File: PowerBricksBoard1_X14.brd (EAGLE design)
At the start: 76.2 x 50.8 mm, 16 parts

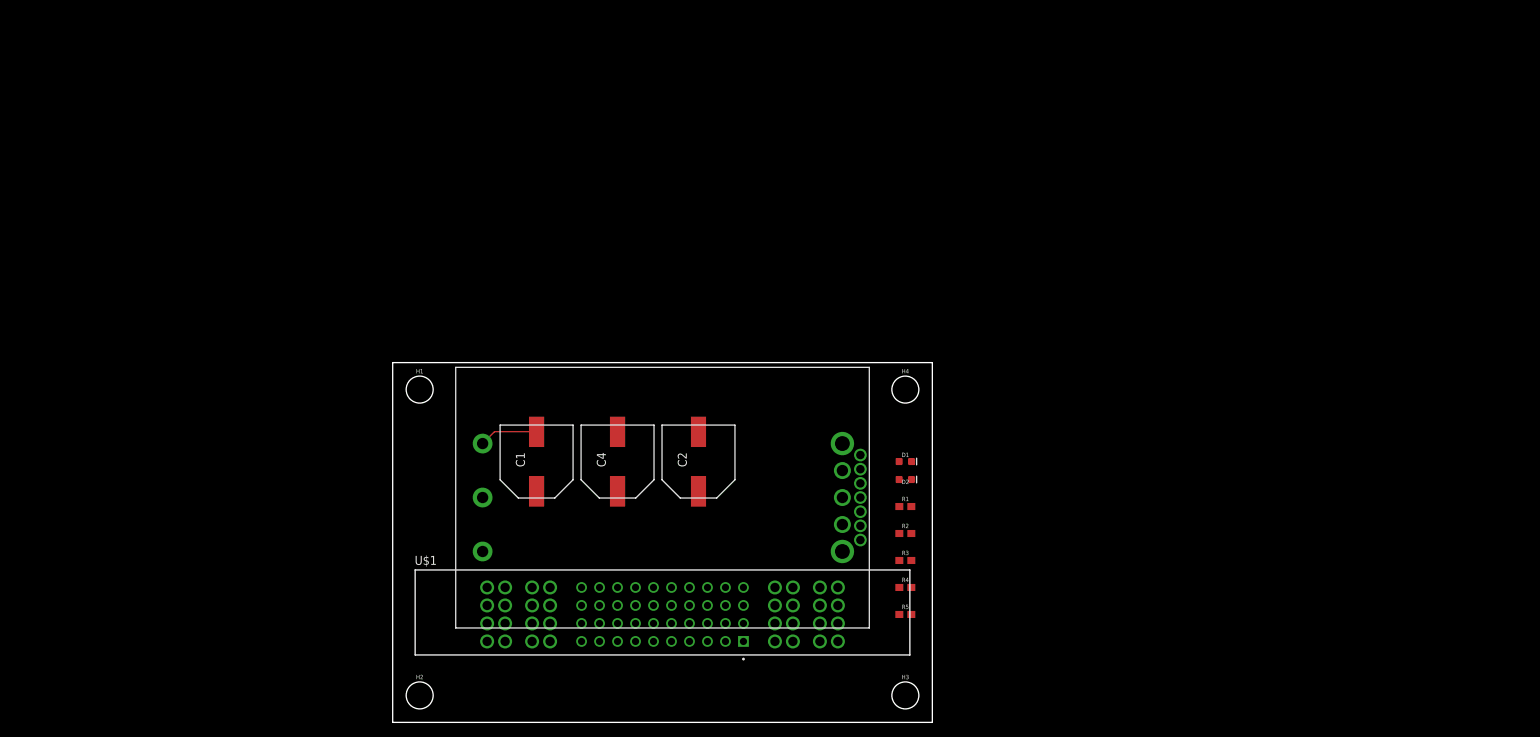
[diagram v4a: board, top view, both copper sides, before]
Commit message: I deleted the old board and made a new one with the connector type.
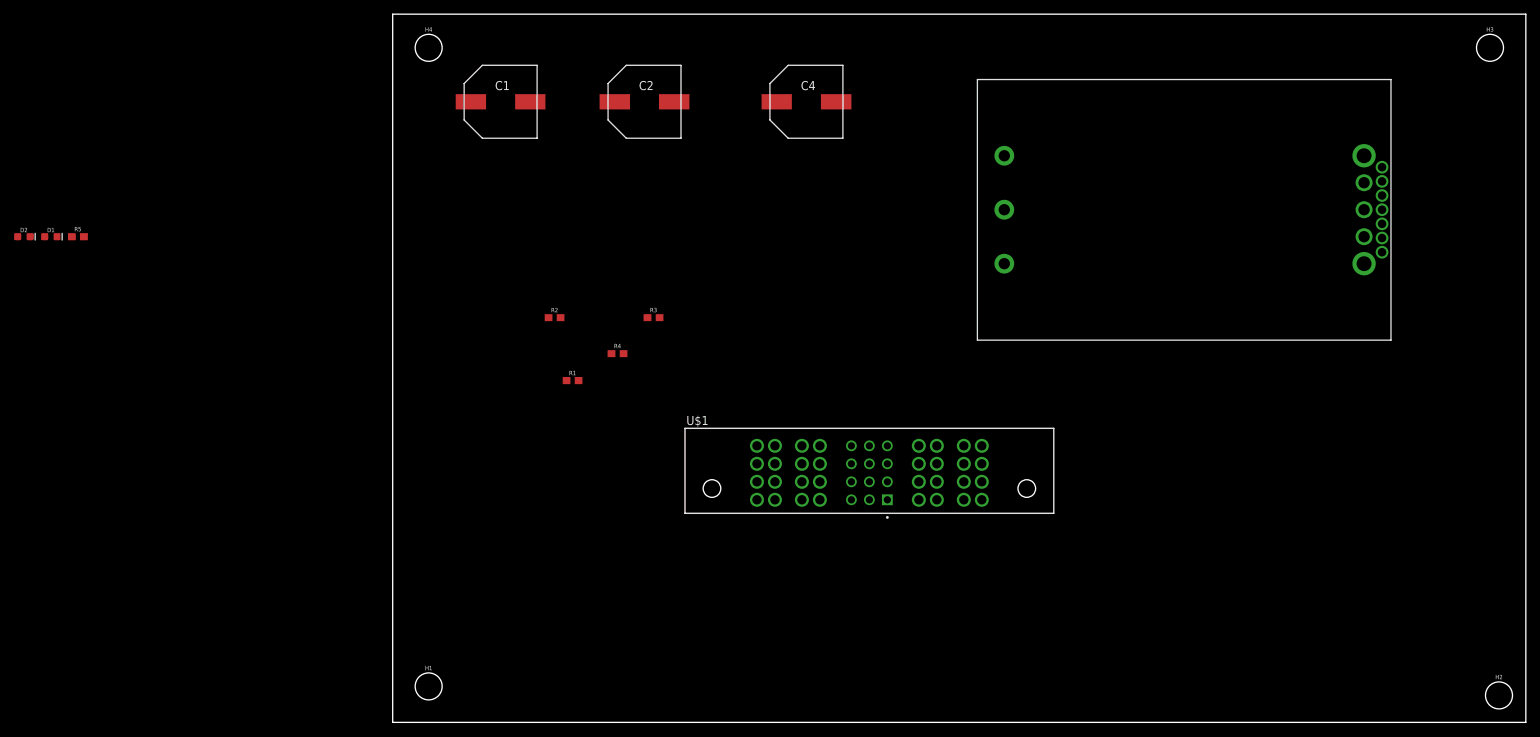
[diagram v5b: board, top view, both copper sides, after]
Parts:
- U$1: value PETC-02-40-01-X-VT(BTOD) -> CONN_BRICKS; device CONN, Distribution-Bricks:SAMTEC_PETC-02-40-01-X-VT_BTOD -> CONN, Distribution-Bricks:SAMTEC_PESC-02-12-02-01-X-VT-LC
- moved H2 152.4 mm to (156.2, 3.81)
- moved D2 129.1 mm to (-52.1, 68.6)
- moved R5 128.4 mm to (-44.5, 68.6)
- moved D1 124.8 mm to (-48.3, 68.6)
- moved H3 123.2 mm to (154.9, 95.2)
- moved U$2 84.1 mm to (86.4, 64.8)
- moved H4 82.8 mm to (5.08, 95.2)
- moved R2 58.2 mm to (22.9, 57.1)
- moved C4 57.4 mm to (58.4, 87.6), turned to 0 degrees
- moved R4 52.4 mm to (31.8, 52.1)
- moved C2 51.4 mm to (35.6, 87.6), turned to 0 degrees
- moved C1 51.1 mm to (15.2, 87.6), turned to 0 degrees
- moved R1 50.2 mm to (25.4, 48.3)
- moved R3 49.4 mm to (36.8, 57.1)
- moved U$1 44.1 mm to (67.3, 33.0)
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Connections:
- removed net 48VGND: U$1.01, U$1.02, U$1.03, U$1.04, U$1.05, U$1.06, U$1.07, U$1.08, U$1.09, U$1.10, U$1.11, U$1.12
- net 12V: no longer U$1.P02_1, U$1.P02_2, U$1.P02_3, U$1.P02_4, U$1.P02_5, U$1.P02_6, U$1.P02_7, U$1.P02_8
- net 12VGND: now also U$1.P02_1, U$1.P02_2, U$1.P02_3, U$1.P02_4, U$1.P02_5, U$1.P02_6, U$1.P02_7, U$1.P02_8; no longer U$1.P03_1, U$1.P03_2, U$1.P03_3, U$1.P03_4, U$1.P03_5, U$1.P03_6, U$1.P03_7, U$1.P03_8, U$1.P04_1, U$1.P04_2, U$1.P04_3, U$1.P04_4, U$1.P04_5, U$1.P04_6, U$1.P04_7, U$1.P04_8
- net 48V: now also U$1.P03_1, U$1.P03_2, U$1.P03_3, U$1.P03_4, U$1.P03_5, U$1.P03_6, U$1.P03_7, U$1.P03_8; no longer U$1.29, U$1.30, U$1.31, U$1.32, U$1.33, U$1.34, U$1.35, U$1.36, U$1.37, U$1.38, U$1.39, U$1.40
- net 48_GND: now also U$1.P04_1, U$1.P04_2, U$1.P04_3, U$1.P04_4, U$1.P04_5, U$1.P04_6, U$1.P04_7, U$1.P04_8
- net ALERT: now also U$1.01; no longer U$1.17
- net C2: now also U$1.02; no longer U$1.18
- net CLK: now also U$1.03; no longer U$1.19
- net DATA: now also U$1.04; no longer U$1.20
- net ON/OFF: now also U$1.05; no longer U$1.21
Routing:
- net 48_GND: track 8.31 -> 0.00 mm
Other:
- board size 76.2 x 50.8 mm -> 160 x 100 mm
